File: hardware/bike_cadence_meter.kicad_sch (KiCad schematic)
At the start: 16 parts, among them J1 3034, J2 1x04, SW1 SW_Push, U2 LSM6DS3, Y1 CM130_9pf_+-20ppm

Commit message: Add manufacturing files
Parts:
- added TP1, TP2, TP3, TP4: TestPoint, TestPoint:TestPoint_Pad_D1.0mm, symbol Connector:TestPoint
- C1, C2: JLPCB # (none) -> C14663
- C5, C6: JLPCB # (none) -> C38523
- D1: JLPCB # (none) -> C2286
- R1, R2, R4: JLPCB # (none) -> C23162
- R3: JLPCB # (none) -> C23162; LCSC (none) -> C23162
- R5: JLPCB # (none) -> C22775
- SW1: JLPCB # (none) -> C318884
- U2: JLPCB # (none) -> C967633
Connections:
- net GND: now also TP2.1
- net INT_1: now also TP4.1
- net VCC: now also TP3.1
- net at U1.13 (I/O): now also TP1.1

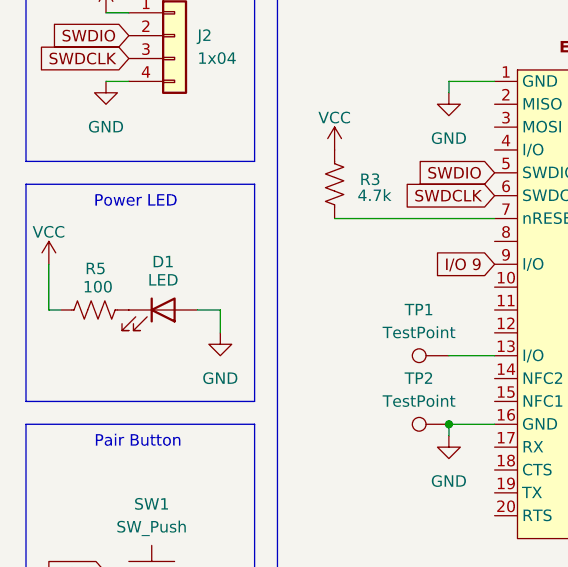
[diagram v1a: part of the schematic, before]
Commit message: Fixed reversed LED
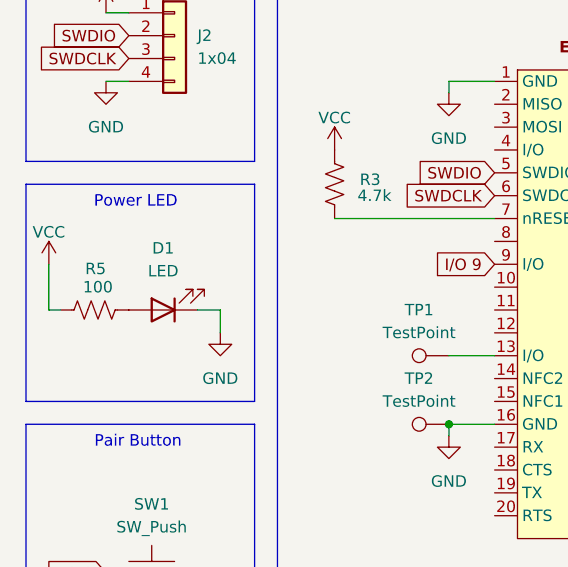
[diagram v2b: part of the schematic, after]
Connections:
- net GND: now also D1.1 (K); no longer D1.2 (A)
- net at R5.2: now also D1.2 (A); no longer D1.1 (K)
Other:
- moved on the sheet: D1
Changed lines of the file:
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@@
 	(symbol
 		(lib_id "Device:LED")
-		(at 29.21 62.23 0)
+		(at 29.21 62.23 180)
 		(unit 1)
 		(exclude_from_sim no)
@@
 		(dnp no)
 		(property "Reference" "D1"
-			(at 29.21 56.896 0)
+			(at 29.21 55.372 0)
 			(effects
 				(font
@@
 		)
 		(property "Value" "LED"
-			(at 29.21 58.928 0)
+			(at 29.21 57.912 0)
 			(effects
 				(font
